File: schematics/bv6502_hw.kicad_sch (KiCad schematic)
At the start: 0 parts

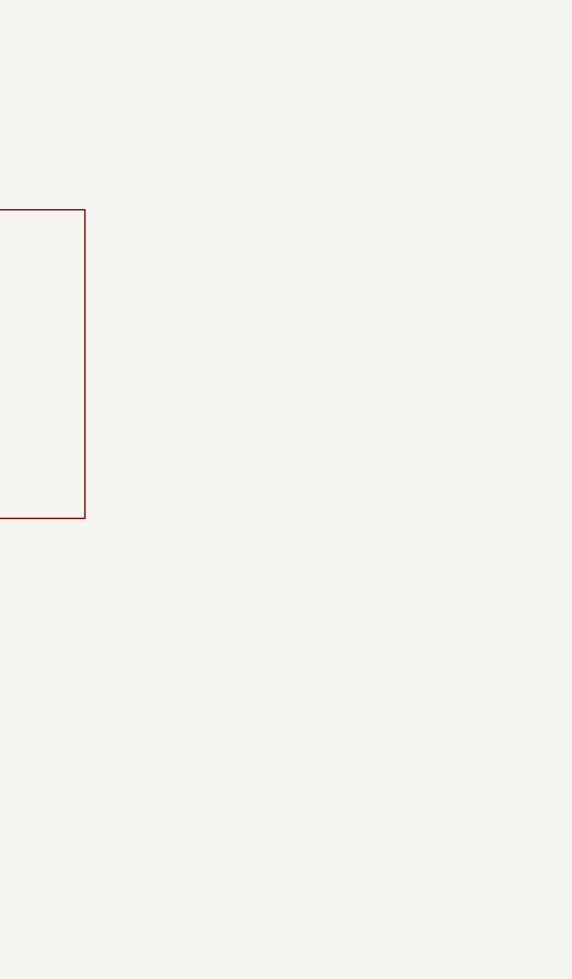
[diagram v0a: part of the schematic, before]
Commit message: Address decoder pld file and no-VIA keyboard schematic and pld file.
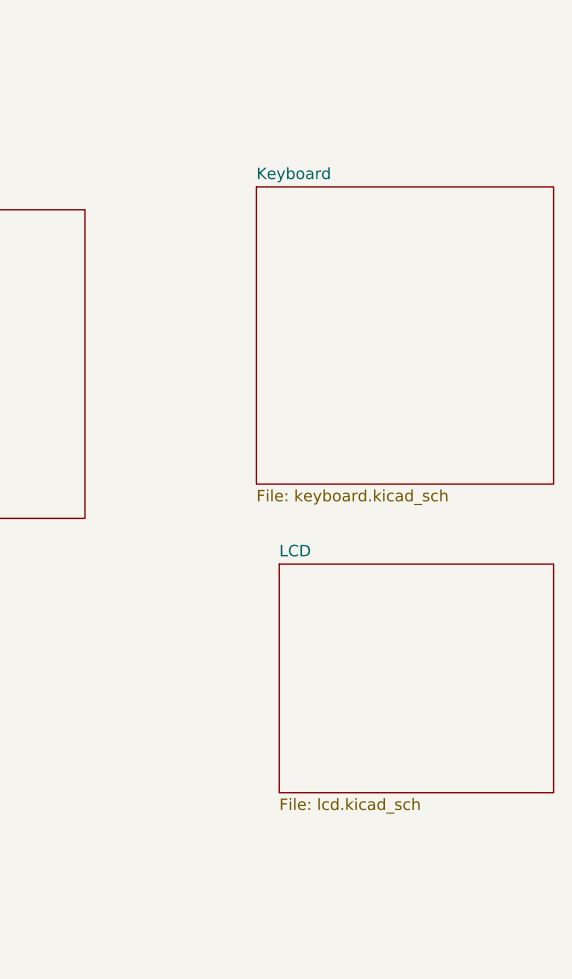
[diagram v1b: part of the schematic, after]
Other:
- added sheet Keyboard (keyboard.kicad_sch)
- added sheet LCD (lcd.kicad_sch)
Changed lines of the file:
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@@
+	)
+	(sheet
+		(at 227.33 99.06)
+		(size 33.02 33.02)
+		(exclude_from_sim no)
+		(in_bom yes)
+		(on_board yes)
+		(dnp no)
+		(fields_autoplaced yes)
+		(stroke
+			(width 0.1524)
+			(type solid)
+		)
+		(fill
+			(color 0 0 0 0)
+		)
+		(property "Sheetname" "Keyboard"
+			(at 227.33 98.3484 0)
+			(show_name no)
+			(do_not_autoplace no)
+			(effects
+				(font
+					(size 1.27 1.27)
+				)
+				(justify left bottom)
+			)
+		)
+		(property "Sheetfile" "keyboard.kicad_sch"
+			(at 227.33 132.6646 0)
+			(show_name no)
+			(do_not_autoplace no)
+			(effects
+				(font
+					(size 1.27 1.27)
+				)
+				(justify left top)
+			)
+		)
+		(instances
+			(project "bv6502_hw"
+				(path "/94c72abe-aaa5-49aa-8ab7-5d3e7cbc10be"
+					(page "8")
+				)
+			)
+		)
+	)
+	(sheet
+		(at 229.87 140.97)
+		(size 30.48 25.4)
+		(exclude_from_sim no)
+		(in_bom yes)
+		(on_board yes)
+		(dnp no)
+		(fields_autoplaced yes)
+		(stroke
+			(width 0.1524)
+			(type solid)
+		)
+		(fill
+			(color 0 0 0 0)
+		)
+		(property "Sheetname" "LCD"
+			(at 229.87 140.2584 0)
+			(show_name no)
+			(do_not_autoplace no)
+			(effects
+				(font
+					(size 1.27 1.27)
+				)
+				(justify left bottom)
+			)
+		)
+		(property "Sheetfile" "lcd.kicad_sch"
+			(at 229.87 166.9546 0)
+			(show_name no)
+			(do_not_autoplace no)
+			(effects
+				(font
+					(size 1.27 1.27)
+				)
+				(justify left top)
+			)
+		)
+		(instances
+			(project "bv6502_hw"
+				(path "/94c72abe-aaa5-49aa-8ab7-5d3e7cbc10be"
+					(page "9")
+				)
+			)
+		)
 	)
 	(sheet

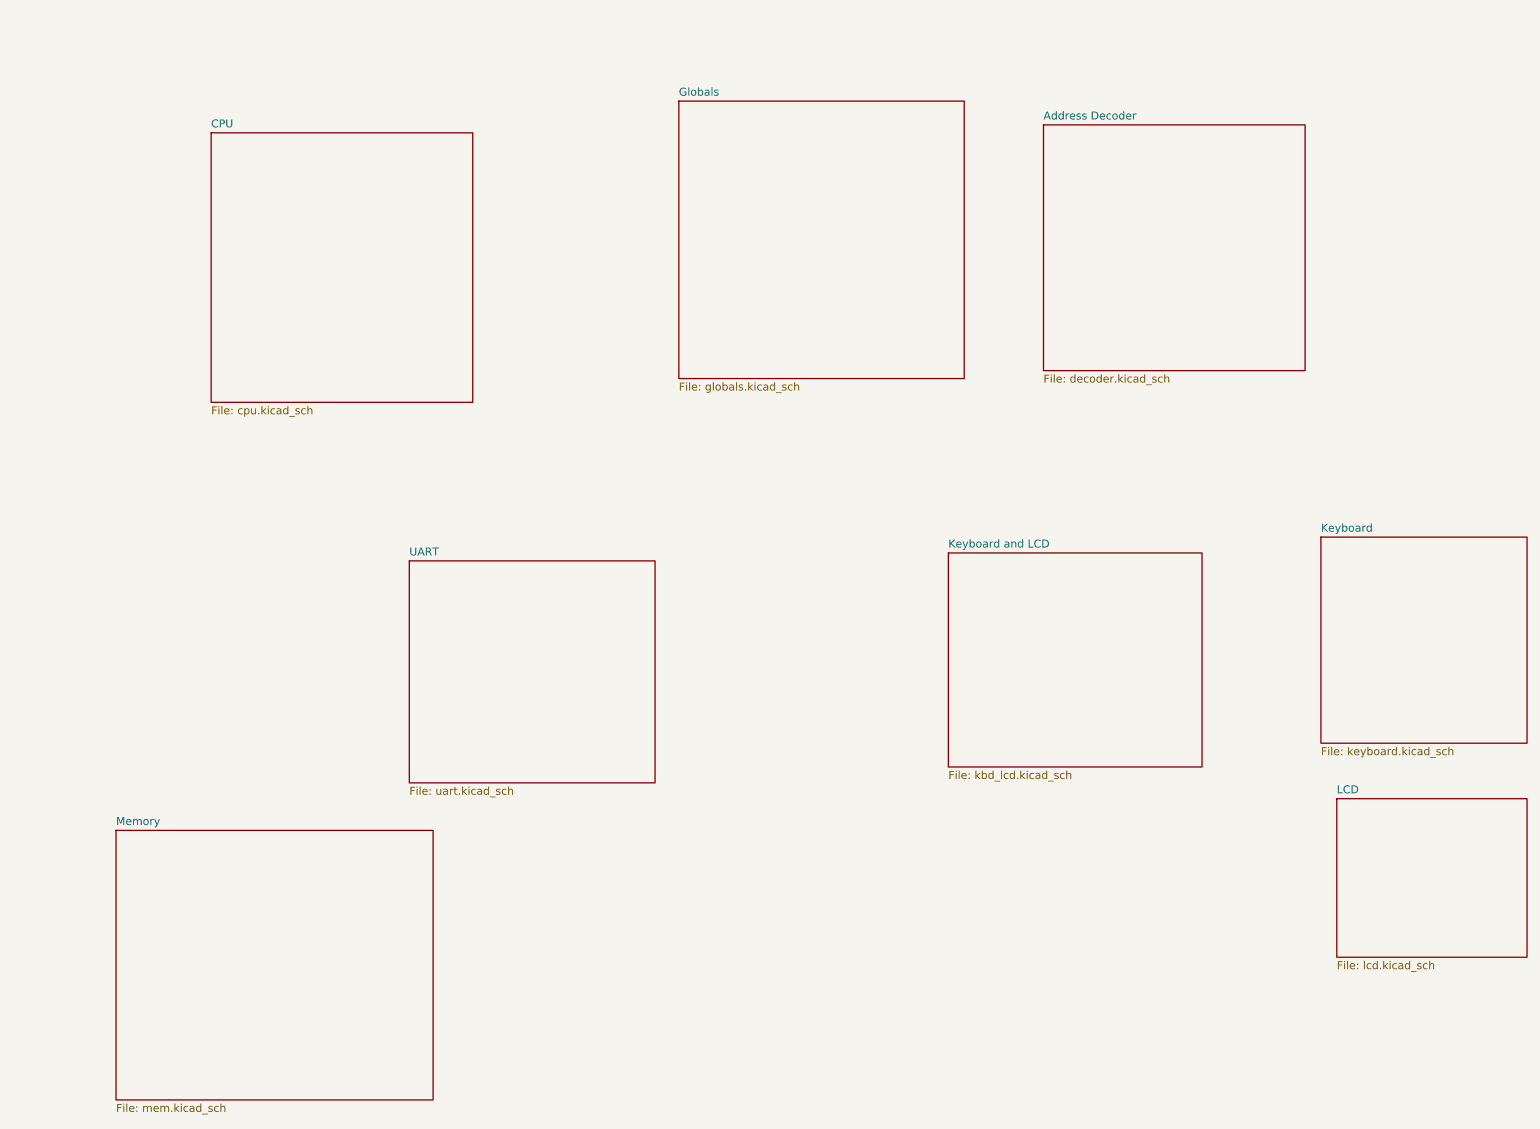
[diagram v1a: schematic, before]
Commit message: PLD files and schematics for address decoder, device selector, keyboard controller, lcd controller, banked memory, and bootloader.
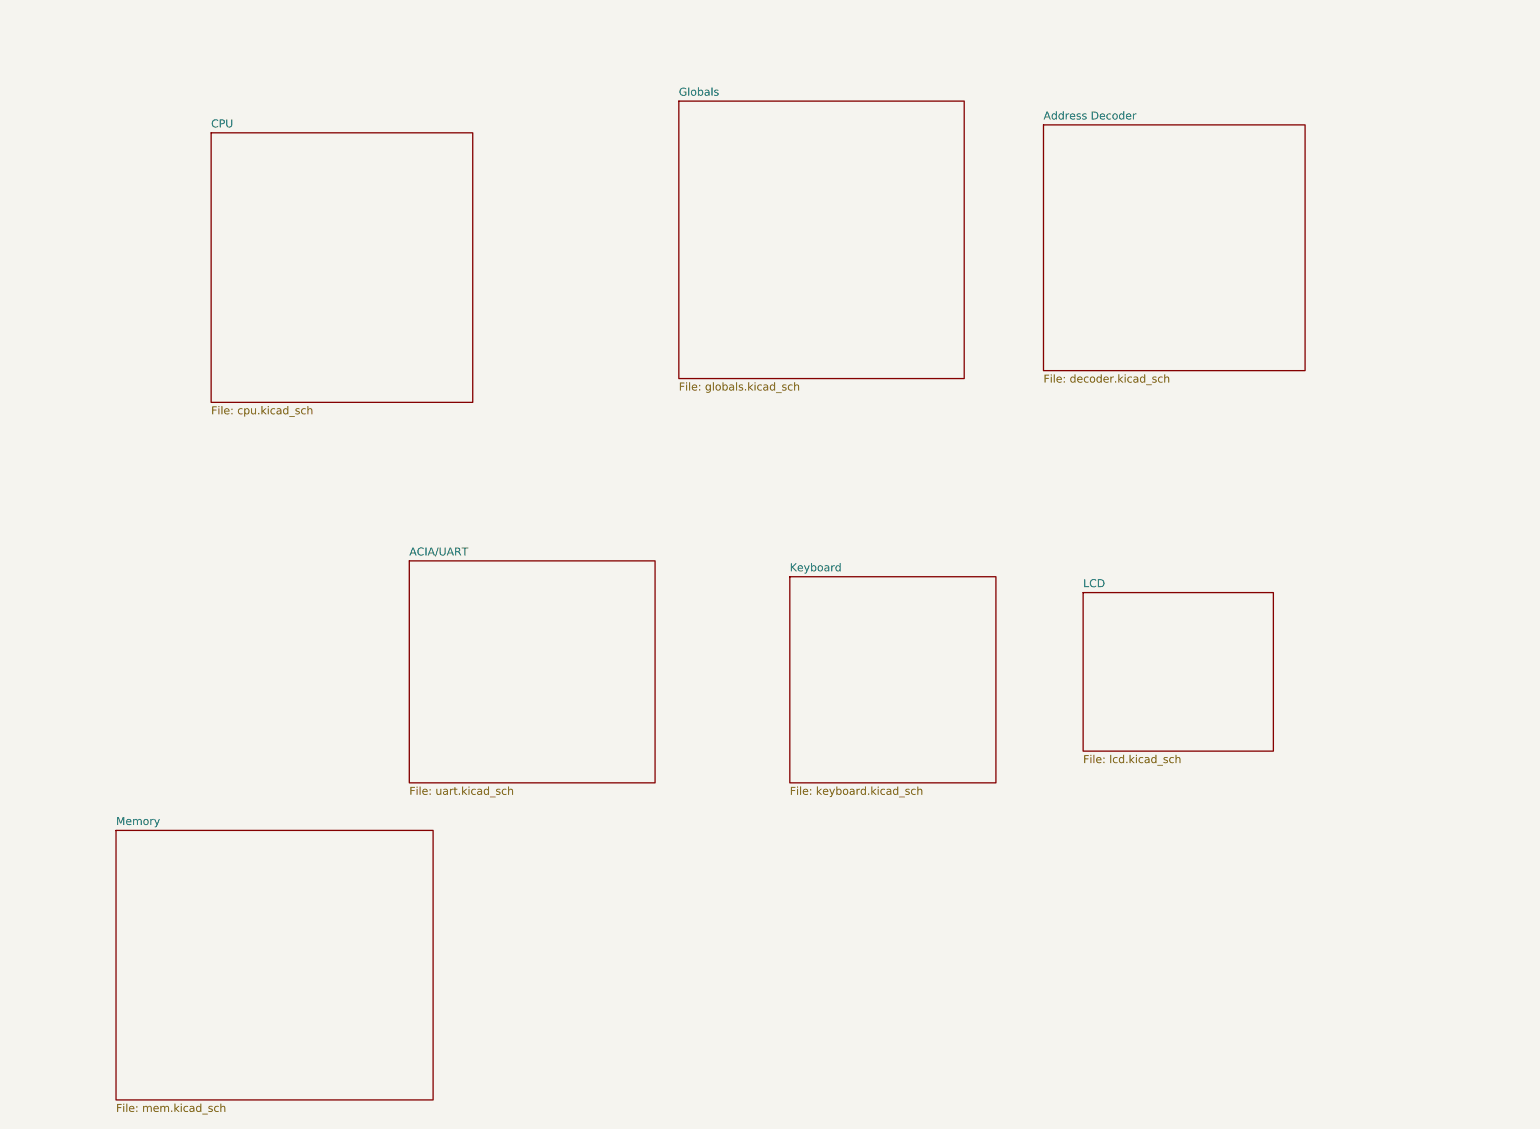
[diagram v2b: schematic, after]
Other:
- sheet UART renamed ACIA/UART
- removed sheet Keyboard and LCD
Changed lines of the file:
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@@
 	(paper "USLetter")
-	(sheet
-		(at 167.64 101.6)
-		(size 40.64 34.29)
-		(exclude_from_sim no)
-		(in_bom yes)
-		(on_board yes)
-		(dnp no)
-		(fields_autoplaced yes)
-		(stroke
-			(width 0.1524)
-			(type solid)
-		)
-		(fill
-			(color 0 0 0 0)
-		)
-		(property "Sheetname" "Keyboard and LCD"
-			(at 167.64 100.8884 0)
-			(show_name no)
-			(do_not_autoplace no)
-			(effects
-				(font
-					(size 1.27 1.27)
-				)
-				(justify left bottom)
-			)
-		)
-		(property "Sheetfile" "kbd_lcd.kicad_sch"
-			(at 167.64 136.4746 0)
-			(show_name no)
-			(do_not_autoplace no)
-			(effects
-				(font
-					(size 1.27 1.27)
-				)
-				(justify left top)
-			)
-		)
-		(instances
-			(project "bv6502_hw"
-				(path "/94c72abe-aaa5-49aa-8ab7-5d3e7cbc10be"
-					(page "7")
-				)
-			)
-		)
-	)
 	(sheet
 		(at 124.46 29.21)
@@
 			(color 0 0 0 0)
 		)
-		(property "Sheetname" "UART"
+		(property "Sheetname" "ACIA/UART"
 			(at 81.28 102.1584 0)
 			(show_name no)
@@
 	)
 	(sheet
-		(at 227.33 99.06)
+		(at 142.24 105.41)
 		(size 33.02 33.02)
 		(exclude_from_sim no)
@@
 		)
 		(property "Sheetname" "Keyboard"
-			(at 227.33 98.3484 0)
+			(at 142.24 104.6984 0)
 			(show_name no)
 			(do_not_autoplace no)
@@
 		)
 		(property "Sheetfile" "keyboard.kicad_sch"
-			(at 227.33 132.6646 0)
+			(at 142.24 139.0146 0)
 			(show_name no)
 			(do_not_autoplace no)
@@
 	)
 	(sheet
-		(at 229.87 140.97)
+		(at 189.23 107.95)
 		(size 30.48 25.4)
 		(exclude_from_sim no)
@@
 		)
 		(property "Sheetname" "LCD"
-			(at 229.87 140.2584 0)
+			(at 189.23 107.2384 0)
 			(show_name no)
 			(do_not_autoplace no)
@@
 		)
 		(property "Sheetfile" "lcd.kicad_sch"
-			(at 229.87 166.9546 0)
-			(show_name no)
-			(do_not_autoplace no)
+			(at 189.23 133.9346 0)
+			(show_name no)
+			(do_not_autoplace no)

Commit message: keyboard, via, acia updates, ready to test
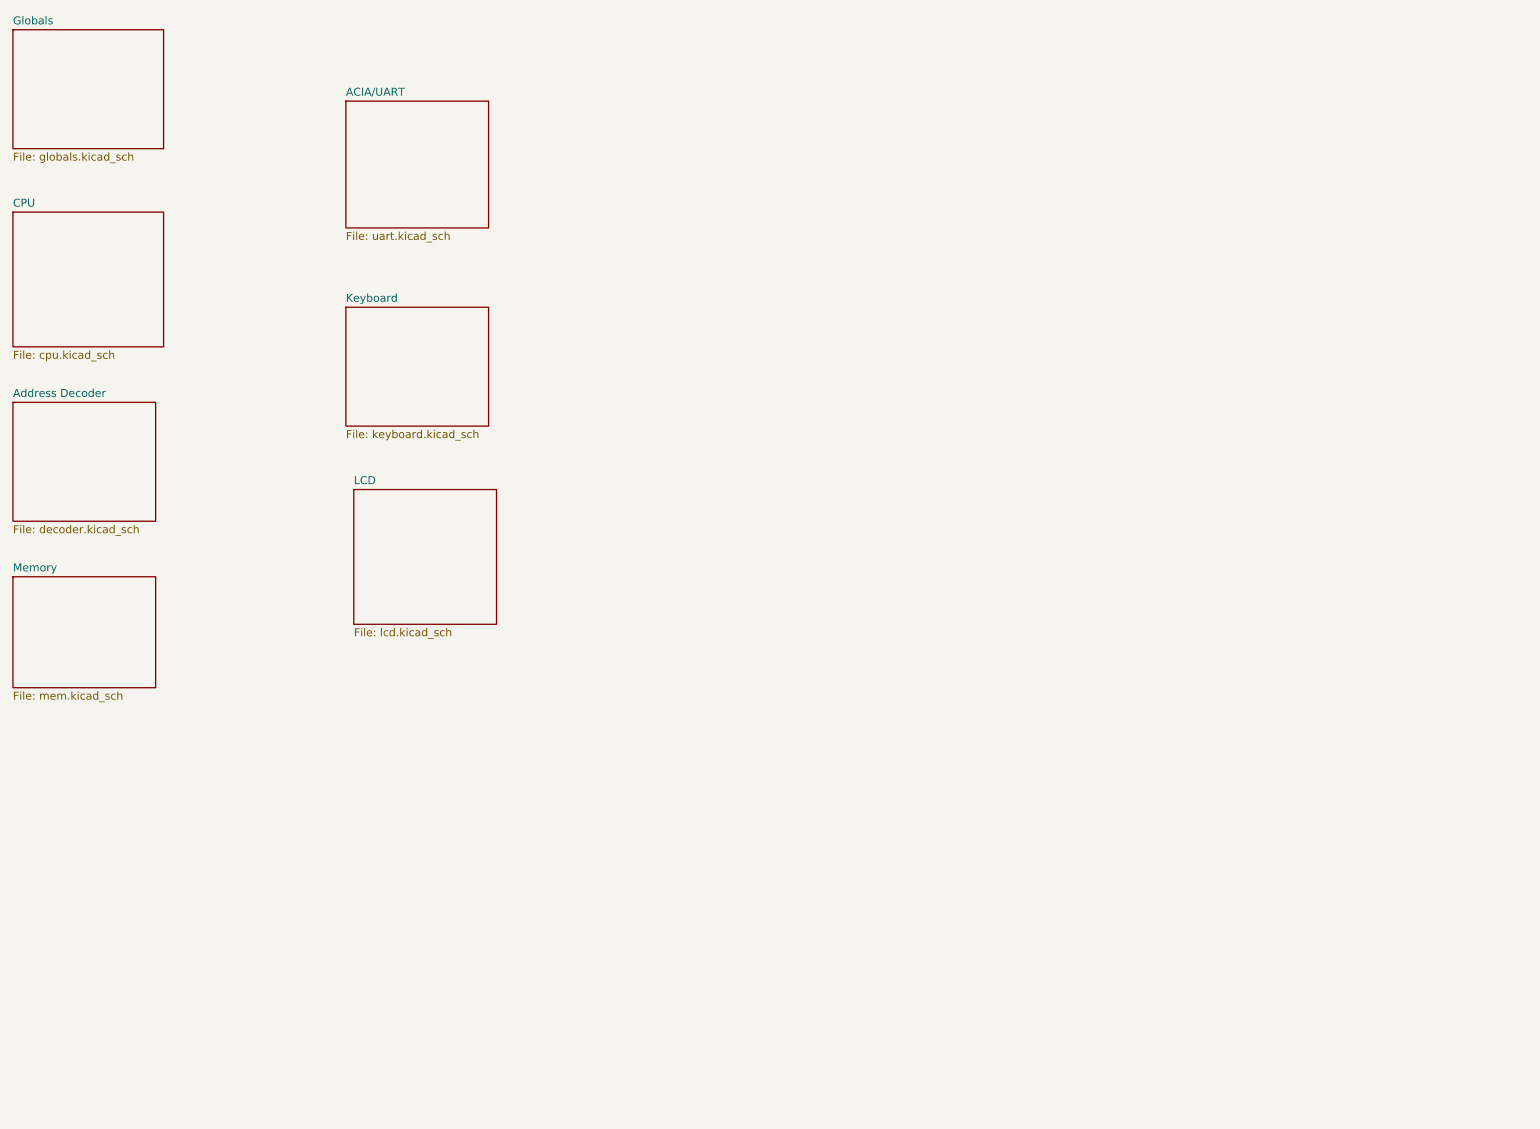
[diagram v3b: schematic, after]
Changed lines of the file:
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@@
 	(paper "USLetter")
 	(sheet
-		(at 124.46 29.21)
-		(size 45.72 44.45)
+		(at 17.78 17.78)
+		(size 24.13 19.05)
 		(exclude_from_sim no)
 		(in_bom yes)
@@
 		)
 		(property "Sheetname" "Globals"
-			(at 124.46 28.4984 0)
+			(at 17.78 17.0684 0)
 			(show_name no)
 			(do_not_autoplace no)
@@
 		)
 		(property "Sheetfile" "globals.kicad_sch"
-			(at 124.46 74.2446 0)
+			(at 17.78 37.4146 0)
 			(show_name no)
 			(do_not_autoplace no)
@@
 	)
 	(sheet
-		(at 81.28 102.87)
-		(size 39.37 35.56)
+		(at 71.12 29.21)
+		(size 22.86 20.32)
 		(exclude_from_sim no)
 		(in_bom yes)
@@
 		)
 		(property "Sheetname" "ACIA/UART"
-			(at 81.28 102.1584 0)
+			(at 71.12 28.4984 0)
 			(show_name no)
 			(do_not_autoplace no)
@@
 		)
 		(property "Sheetfile" "uart.kicad_sch"
-			(at 81.28 139.0146 0)
+			(at 71.12 50.1146 0)
 			(show_name no)
 			(do_not_autoplace no)
@@
 	)
 	(sheet
-		(at 182.88 33.02)
-		(size 41.91 39.37)
+		(at 17.78 77.47)
+		(size 22.86 19.05)
 		(exclude_from_sim no)
 		(in_bom yes)
@@
 		)
 		(property "Sheetname" "Address Decoder"
-			(at 182.88 32.3084 0)
+			(at 17.78 76.7584 0)
 			(show_name no)
 			(do_not_autoplace no)
@@
 		)
 		(property "Sheetfile" "decoder.kicad_sch"
-			(at 182.88 72.9746 0)
+			(at 17.78 97.1046 0)
 			(show_name no)
 			(do_not_autoplace no)
@@
 	)
 	(sheet
-		(at 142.24 105.41)
-		(size 33.02 33.02)
+		(at 71.12 62.23)
+		(size 22.86 19.05)
 		(exclude_from_sim no)
 		(in_bom yes)
@@
 		)
 		(property "Sheetname" "Keyboard"
-			(at 142.24 104.6984 0)
+			(at 71.12 61.5184 0)
 			(show_name no)
 			(do_not_autoplace no)
@@
 		)
 		(property "Sheetfile" "keyboard.kicad_sch"
-			(at 142.24 139.0146 0)
+			(at 71.12 81.8646 0)
 			(show_name no)
 			(do_not_autoplace no)
@@
 	)
 	(sheet
-		(at 189.23 107.95)
-		(size 30.48 25.4)
+		(at 72.39 91.44)
+		(size 22.86 21.59)
 		(exclude_from_sim no)
 		(in_bom yes)
@@
 		)
 		(property "Sheetname" "LCD"
-			(at 189.23 107.2384 0)
+			(at 72.39 90.7284 0)
 			(show_name no)
 			(do_not_autoplace no)
@@
 		)
 		(property "Sheetfile" "lcd.kicad_sch"
-			(at 189.23 133.9346 0)
+			(at 72.39 113.6146 0)
 			(show_name no)
 			(do_not_autoplace no)
@@
 	)
 	(sheet
-		(at 34.29 146.05)
-		(size 50.8 43.18)
+		(at 17.78 105.41)
+		(size 22.86 17.78)
 		(exclude_from_sim no)
 		(in_bom yes)
@@
 		)
 		(property "Sheetname" "Memory"
-			(at 34.29 145.3384 0)
+			(at 17.78 104.6984 0)
 			(show_name no)
 			(do_not_autoplace no)
@@
 		)
 		(property "Sheetfile" "mem.kicad_sch"
-			(at 34.29 189.8146 0)
+			(at 17.78 123.7746 0)
 			(show_name no)
 			(do_not_autoplace no)
@@
 	)
 	(sheet
-		(at 49.53 34.29)
-		(size 41.91 43.18)
+		(at 17.78 46.99)
+		(size 24.13 21.59)
 		(exclude_from_sim no)
 		(in_bom yes)
@@
 		)
 		(property "Sheetname" "CPU"
-			(at 49.53 33.5784 0)
+			(at 17.78 46.2784 0)
 			(show_name no)
 			(do_not_autoplace no)
@@
 		)
 		(property "Sheetfile" "cpu.kicad_sch"
-			(at 49.53 78.0546 0)
-			(show_name no)
-			(do_not_autoplace no)
+			(at 17.78 69.1646 0)
+			(show_name no)
+			(do_not_autoplace no)

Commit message: added phi0 for write latch timing
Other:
- added sheet VIA (via.kicad_sch)
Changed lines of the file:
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@@
 	(paper "USLetter")
+	(sheet
+		(at 74.93 130.81)
+		(size 22.86 20.32)
+		(exclude_from_sim no)
+		(in_bom yes)
+		(on_board yes)
+		(dnp no)
+		(fields_autoplaced yes)
+		(stroke
+			(width 0.1524)
+			(type solid)
+		)
+		(fill
+			(color 0 0 0 0)
+		)
+		(property "Sheetname" "VIA"
+			(at 74.93 130.0984 0)
+			(show_name no)
+			(do_not_autoplace no)
+			(effects
+				(font
+					(size 1.27 1.27)
+				)
+				(justify left bottom)
+			)
+		)
+		(property "Sheetfile" "via.kicad_sch"
+			(at 74.93 151.7146 0)
+			(show_name no)
+			(do_not_autoplace no)
+			(effects
+				(font
+					(size 1.27 1.27)
+				)
+				(justify left top)
+			)
+		)
+		(instances
+			(project "bv6502_hw"
+				(path "/94c72abe-aaa5-49aa-8ab7-5d3e7cbc10be"
+					(page "7")
+				)
+			)
+		)
+	)
 	(sheet
 		(at 17.78 17.78)

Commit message: fixing wiring
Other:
- added sheet VGA (vga.kicad_sch)
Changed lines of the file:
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@@
+	)
+	(sheet
+		(at 144.78 80.01)
+		(size 30.48 26.67)
+		(exclude_from_sim no)
+		(in_bom yes)
+		(on_board yes)
+		(dnp no)
+		(fields_autoplaced yes)
+		(stroke
+			(width 0.1524)
+			(type solid)
+		)
+		(fill
+			(color 0 0 0 0)
+		)
+		(property "Sheetname" "VGA"
+			(at 144.78 79.2984 0)
+			(show_name no)
+			(do_not_autoplace no)
+			(effects
+				(font
+					(size 1.27 1.27)
+				)
+				(justify left bottom)
+			)
+		)
+		(property "Sheetfile" "vga.kicad_sch"
+			(at 144.78 107.2646 0)
+			(show_name no)
+			(do_not_autoplace no)
+			(effects
+				(font
+					(size 1.27 1.27)
+				)
+				(justify left top)
+			)
+		)
+		(instances
+			(project "bv6502_hw"
+				(path "/94c72abe-aaa5-49aa-8ab7-5d3e7cbc10be"
+					(page "10")
+				)
+			)
+		)
 	)
 	(sheet
